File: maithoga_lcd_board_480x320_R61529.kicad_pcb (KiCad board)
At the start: 2 copper layers, 85 x 54.5 mm, 22 parts, among them P1 Display Connector, P2 LicheePi_Con, P3 TouchXY Connector, U1 TSC2007, U2 DIO5661ST6

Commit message: Tracking finished
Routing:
- net 3V3: track 15.9 -> 157.7 mm, vias 0 -> 7
- net /Display and Touchscreen/DISP_~RESET~: track 1.13 -> 107.8 mm, vias 1 -> 4
- net /Display and Touchscreen/BACKLIGHT_PWM: track 0.00 -> 98.4 mm, vias 0 -> 4
- net /Display and Touchscreen/DISP_D0: track 0.00 -> 97.9 mm, vias 0 -> 3
- net /Display and Touchscreen/DISP_D3: track 0.00 -> 96.1 mm, vias 0 -> 2
- net /Display and Touchscreen/DISP_D1: track 0.00 -> 95.9 mm, vias 0 -> 2
- net /Display and Touchscreen/LCD_LED_A: track 8.60 -> 104.5 mm, vias 0 -> 2
- net /Display and Touchscreen/DISP_D2: track 0.00 -> 95.7 mm, vias 0 -> 3
- net /Display and Touchscreen/DISP_D5: track 0.00 -> 95.3 mm, vias 0 -> 2
- net /Display and Touchscreen/DISP_D4: track 0.00 -> 94.3 mm, vias 0 -> 3
- net /Display and Touchscreen/DISP_D13: track 0.00 -> 94.3 mm, vias 0 -> 2
- net /Display and Touchscreen/DISP_D9: track 0.00 -> 94.0 mm, vias 0 -> 2
- net /Display and Touchscreen/DISP_D6: track 0.00 -> 91.6 mm, vias 0 -> 3
- net /Lichee Pi Display Connector/TPX1: track 10.7 -> 102.2 mm, vias 0 -> 4
- net /Display and Touchscreen/DISP_D8: track 0.00 -> 89.8 mm, vias 0 -> 3
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- added copper zone on B.Cu, net GND
- added copper zone on F.Cu, net GND

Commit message: Generated gerbers
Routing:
- net /Display and Touchscreen/DISP_~RESET~: track 107.8 -> 106.0 mm
- net /Display and Touchscreen/LCD_LED_K: track 98.7 -> 97.6 mm
- net /Display and Touchscreen/DISP_D1: track 95.9 -> 96.4 mm

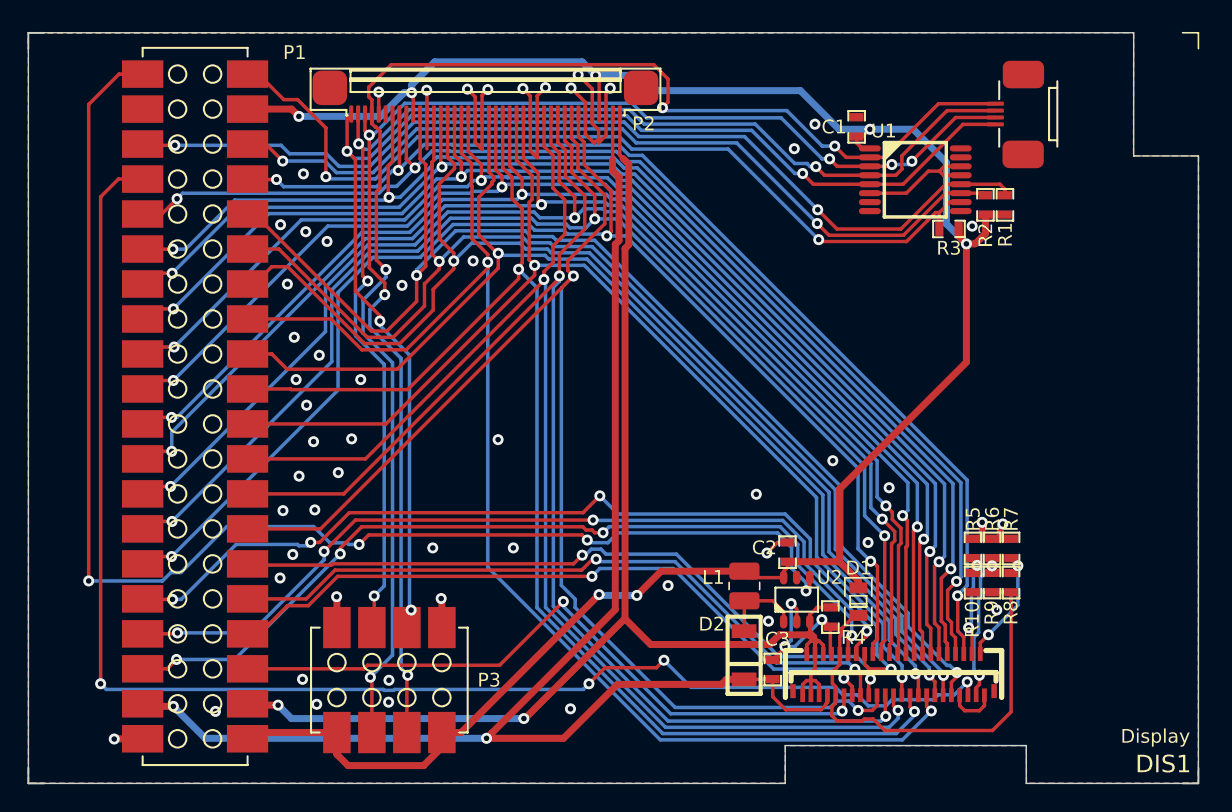
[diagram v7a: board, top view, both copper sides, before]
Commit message: Added new capacitive display
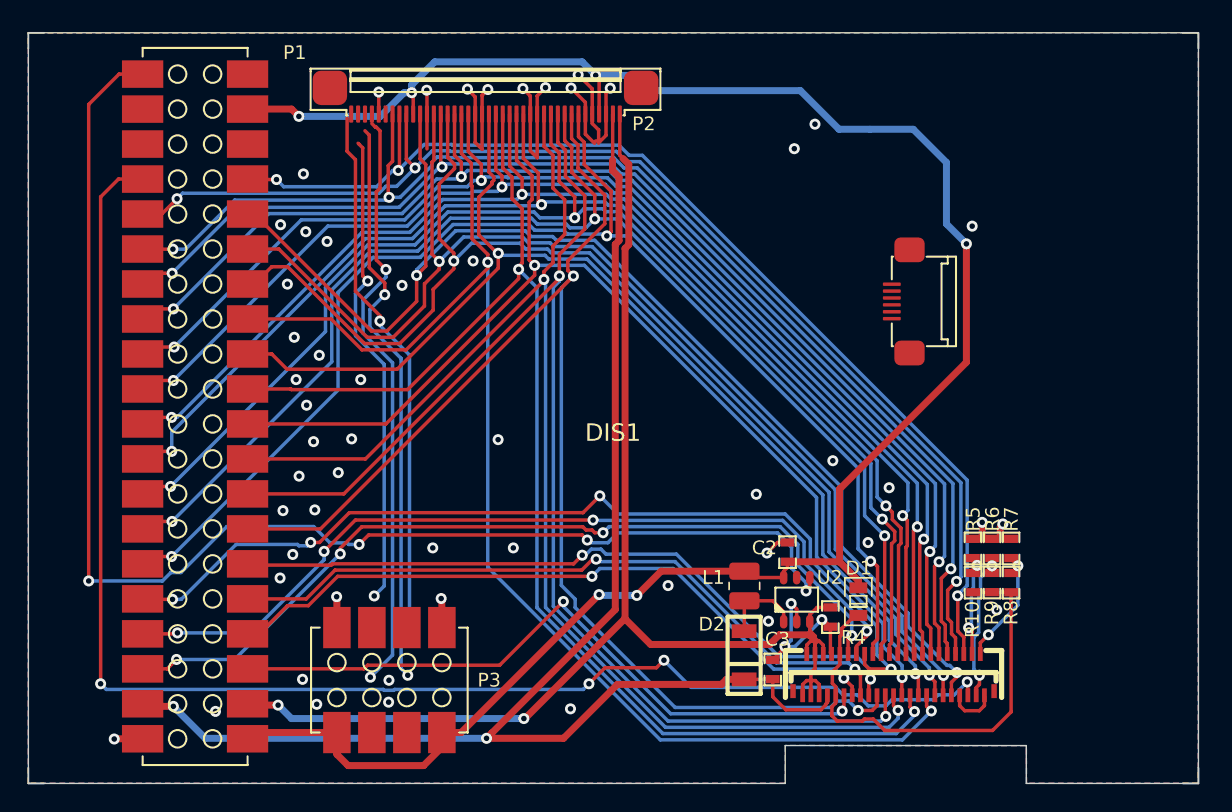
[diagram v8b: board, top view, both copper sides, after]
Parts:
- removed C1: 100nF/50V, Capacitors_Smd_0603:100nF_0603
- removed R1, R2: 4k7, Resistor_Smd_0603:4k7_0603
- removed R3: 47k, Resistor_Smd_0603:47k_0603
- removed U1: TSC2007, Touch_Sensors:TSC2007_TSSOP16
- DIS1: value maithoga_rgb_with_resistive_ts -> maithoga_tft_480x320_rgb_with_capacitive_ts; footprint Display_Lcd:maithoga_tft_480x320_rgb_with_resistive_ts -> Display_Lcd:maithoga_tft_480x320_rgb_with_capacitive_ts
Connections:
- P1 pad 35: /Display and Touchscreen/TOUCHSCREEN_SDA -> (no net)
- P1 pad 36: /Display and Touchscreen/TOUCHSCREEN_SCL -> (no net)
- P1 pad 39: /Display and Touchscreen/TOUCHSCREEN_IRQ -> (no net)
- P2 pad 1: /Lichee Pi Display Connector/TPY2 -> (no net)
- P2 pad 2: /Lichee Pi Display Connector/TPX2 -> (no net)
- P2 pad 3: /Lichee Pi Display Connector/TPY1 -> (no net)
- P2 pad 4: /Lichee Pi Display Connector/TPX1 -> (no net)
- P3 pad 3: /Lichee Pi Display Connector/TPX1 -> (no net)
- P3 pad 4: /Lichee Pi Display Connector/TPX2 -> (no net)
- P3 pad 5: /Lichee Pi Display Connector/TPY1 -> (no net)
- P3 pad 6: /Lichee Pi Display Connector/TPY2 -> (no net)
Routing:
- net /Display and Touchscreen/TOUCHSCREEN_SCL: track 69.8 -> 0.00 mm, vias 2 -> 0
- net /Display and Touchscreen/TOUCHSCREEN_IRQ: track 63.8 -> 0.00 mm, vias 2 -> 0
- net /Display and Touchscreen/TOUCHSCREEN_SDA: track 60.3 -> 0.00 mm, vias 2 -> 0
- net /Lichee Pi Display Connector/TPX1: track 102.3 -> 43.3 mm, vias 4 -> 2
- net /Lichee Pi Display Connector/TPX2: track 91.3 -> 34.7 mm, vias 4 -> 2
- net /Lichee Pi Display Connector/TPY1: track 96.9 -> 41.8 mm, vias 6 -> 2
- net /Lichee Pi Display Connector/TPY2: track 91.9 -> 37.6 mm, vias 4 -> 1
- net GND: track 79.3 -> 70.3 mm
- net 3V3: track 157.7 -> 149.1 mm, vias 7 -> 6
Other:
- outline, holes or cut-outs redrawn
